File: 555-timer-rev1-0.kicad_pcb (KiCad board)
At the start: 2 copper layers, 19 parts, among them J1 Conn_01x02_Male, SW1 SW_Push, SW2 SW_Push, U1 SA555D

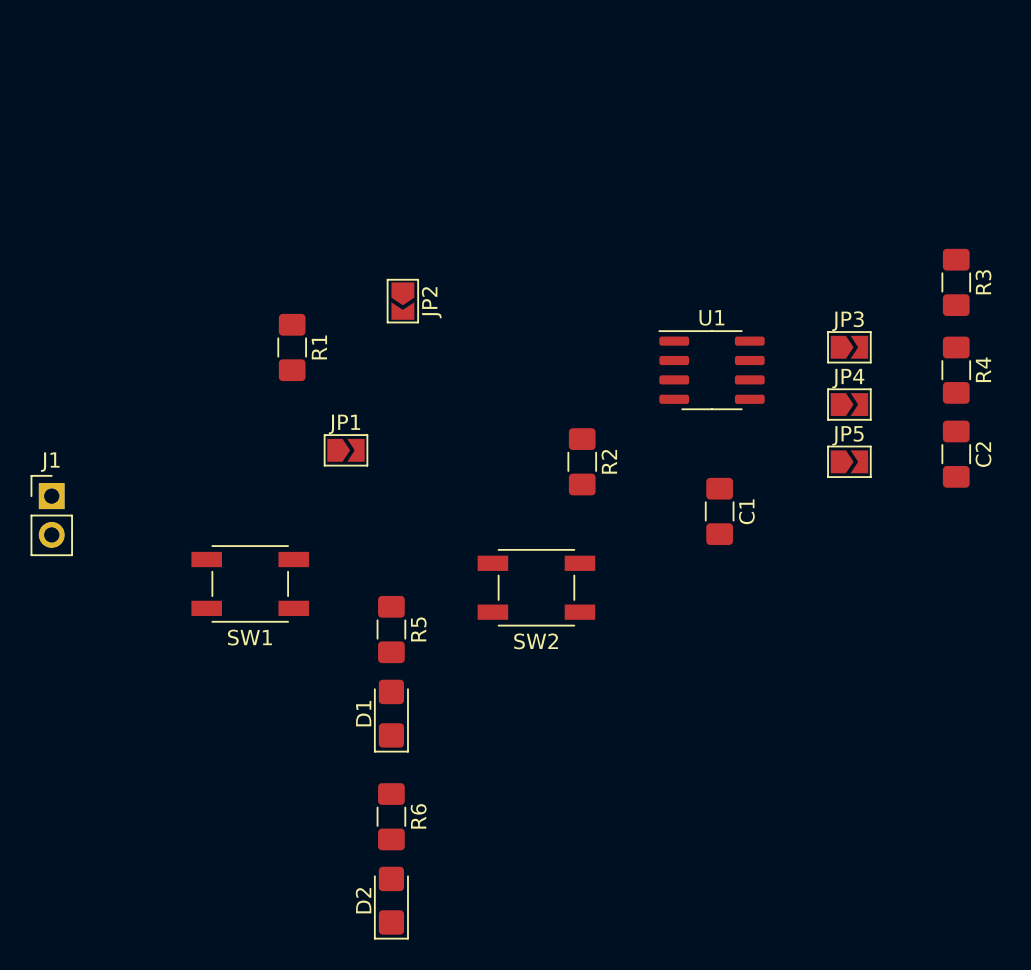
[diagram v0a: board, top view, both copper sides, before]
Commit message: Update PCB layout for 2-layer board.
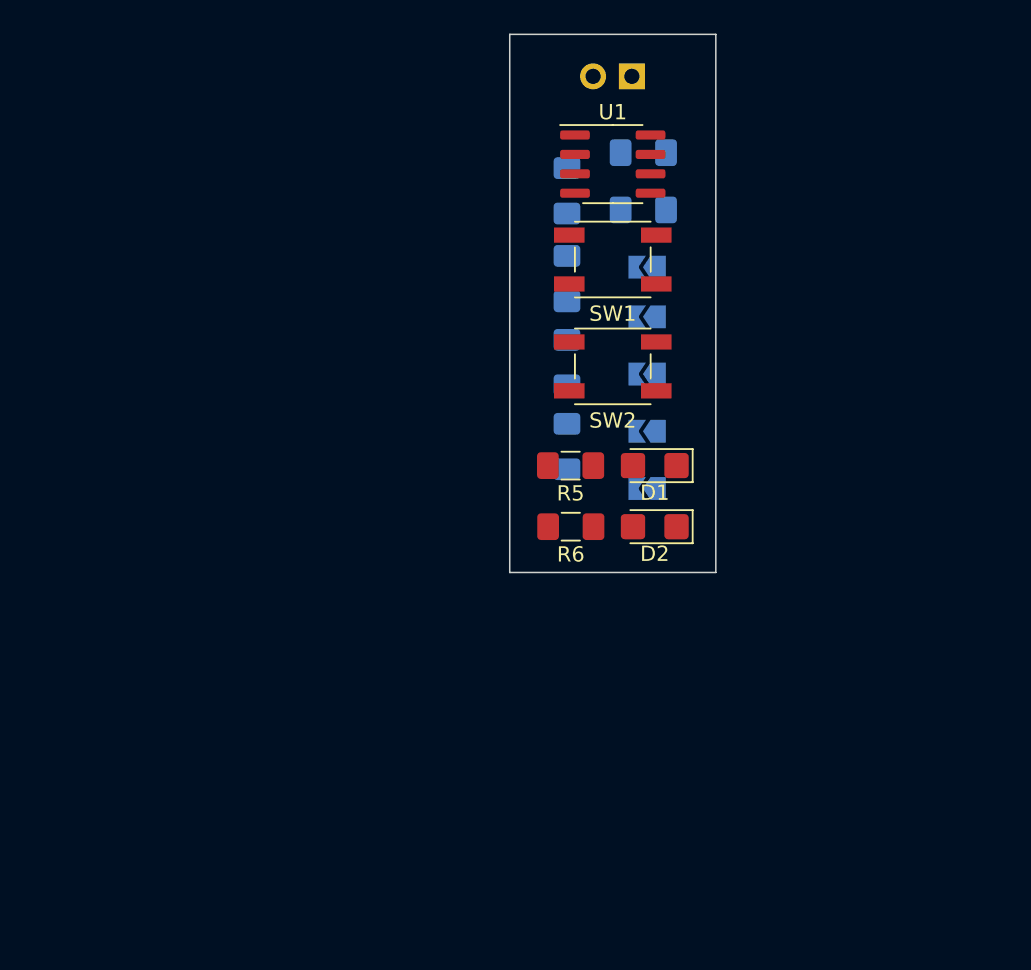
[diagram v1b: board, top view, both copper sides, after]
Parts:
- C1, C2, J1, JP1, JP2, JP3, JP4, JP5, R1, R2, R3, R4: moved to B.Cu
- moved J1 46.9 mm to (150.0, 75.0), turned to 90 degrees
- moved SW1 31.9 mm to (148.8, 87.0)
- moved D2 30.0 mm to (151.5, 104.5), turned to 180 degrees
- moved R1 26.3 mm to (150.8, 80.0), turned to 180 degrees
- moved C2 26.2 mm to (145.8, 93.8)
- moved R3 26.2 mm to (145.8, 82.5)
- moved R4 26.2 mm to (145.8, 88.2)
- moved D1 23.7 mm to (151.5, 100.5), turned to 180 degrees
- moved JP1 23.1 mm to (151.0, 87.5), turned to 180 degrees
- moved R6 22.3 mm to (146.0, 104.5), turned to 180 degrees
- moved JP2 20.2 mm to (151.0, 102.0), turned to 180 degrees
- moved R2 17.0 mm to (150.8, 83.8), turned to 180 degrees
- moved R5 15.9 mm to (146.0, 100.5), turned to 180 degrees
- moved SW2 15.3 mm to (148.8, 94.0)
- moved U1 15.0 mm to (148.8, 80.8)
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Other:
- board outline added: 13.5 x 35.2 mm

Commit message: Finish PCB layout.
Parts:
- moved C1 20.3 mm to (150.5, 79.5), turned to 180 degrees
- moved R2 6.56 mm to (145.8, 79.5), turned to 270 degrees
- moved R5 5.53 mm to (151.5, 100.8), turned to 0 degrees
- moved D1 5.51 mm to (146.0, 100.8), turned to 0 degrees
- moved D2 5.50 mm to (146.0, 104.5), turned to 0 degrees
- moved R6 5.50 mm to (151.5, 104.5), turned to 0 degrees
- moved R1 3.26 mm to (150.5, 83.2)
- moved C2 2.50 mm to (145.8, 96.2)
- moved R3 2.50 mm to (145.8, 85.0)
- moved R4 2.50 mm to (145.8, 90.8)
- moved JP1 0.50 mm to (151.0, 87.0)
- renumbered JP3 to JP2, JP4 to JP3, JP5 to JP4, JP2 to JP5
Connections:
- C2 pad 1: /TRIGGER -> Net-(C2-Pad1)
- JP1 pad 2: Net-(JP1-Pad2) -> /TRIGGER
- JP3 pad 2: /TRIGGER -> Net-(C2-Pad1)
- JP4 pad 2: /TRIGGER -> Net-(C2-Pad1)
- JP5 pad 1: Net-(JP1-Pad1) -> /TRIGGER
- JP5 pad 2: /TRIGGER -> Net-(C2-Pad1)
- R1 pad 1: +5V -> Net-(JP1-Pad1)
- R1 pad 2: Net-(JP1-Pad2) -> +5V
- R4 pad 2: /TRIGGER -> Net-(C2-Pad1)
- R5 pad 1: +5V -> Net-(D1-Pad2)
- R5 pad 2: Net-(D1-Pad2) -> +5V
- R6 pad 1: Net-(D1-Pad1) -> Net-(D2-Pad2)
- R6 pad 2: Net-(D2-Pad2) -> Net-(D1-Pad1)
- SW1 pad 2: Net-(JP1-Pad2) -> Net-(JP1-Pad1)
- U1 pad 2: Net-(JP1-Pad1) -> /TRIGGER
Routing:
- net +5V: track 0.00 -> 54.3 mm
- net GND: track 0.00 -> 53.1 mm, vias 0 -> 1
- net /TRIGGER: track 0.00 -> 40.4 mm, vias 0 -> 1
- net Net-(D1-Pad1): track 0.00 -> 34.3 mm
- net Net-(JP4-Pad1): track 0.00 -> 20.8 mm, vias 0 -> 1
- net Net-(JP2-Pad1): track 0.00 -> 17.2 mm, vias 0 -> 1
- net Net-(R2-Pad2): track 0.00 -> 17.2 mm, vias 0 -> 1
- net Net-(C2-Pad1): track 0.00 -> 14.7 mm
- net Net-(C1-Pad1): track 0.00 -> 11.3 mm, vias 0 -> 1
- net Net-(JP1-Pad1): track 0.00 -> 8.40 mm, vias 0 -> 1
- net Net-(JP2-Pad2): track 0.00 -> 7.92 mm
- net Net-(D1-Pad2): track 0.00 -> 2.60 mm
- net Net-(D2-Pad2): track 0.00 -> 2.59 mm
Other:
- board size 13.5 x 35.2 mm -> 14 x 35.2 mm

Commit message: Add name to silkscreen.
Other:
- board text added: "555 Timer - Rev 1-0 Alexander Fraser 9 Aug 2020"
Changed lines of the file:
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@@
   (general
     (thickness 1.6)
-    (drawings 4)
+    (drawings 5)
     (tracks 110)
     (zones 0)
@@
     )
   )
+  (gr_text "555 Timer - Rev 1-0\nAlexander Fraser\n9 Aug 2020" (at 148.75 105.5) (layer B.SilkS)
+    (effects (font (size 0.5 0.5) (thickness 0.125)) (justify mirror))
+  )
   (gr_line (start 155.75 72.25) (end 155.75 107.5) (layer Edge.Cuts) (width 0.1))

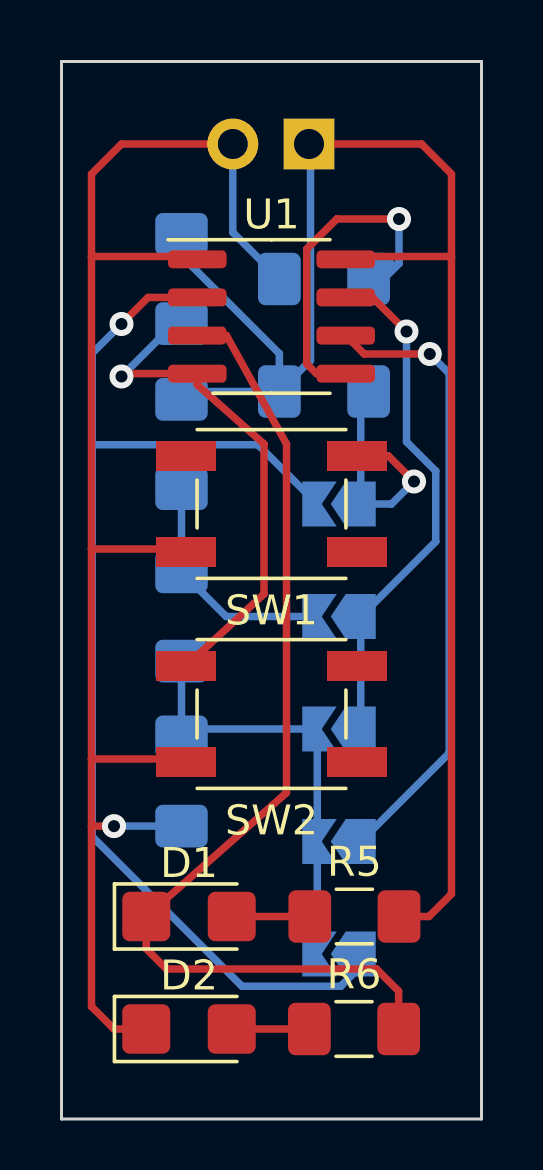
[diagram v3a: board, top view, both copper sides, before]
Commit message: Reverse power rail orientation.
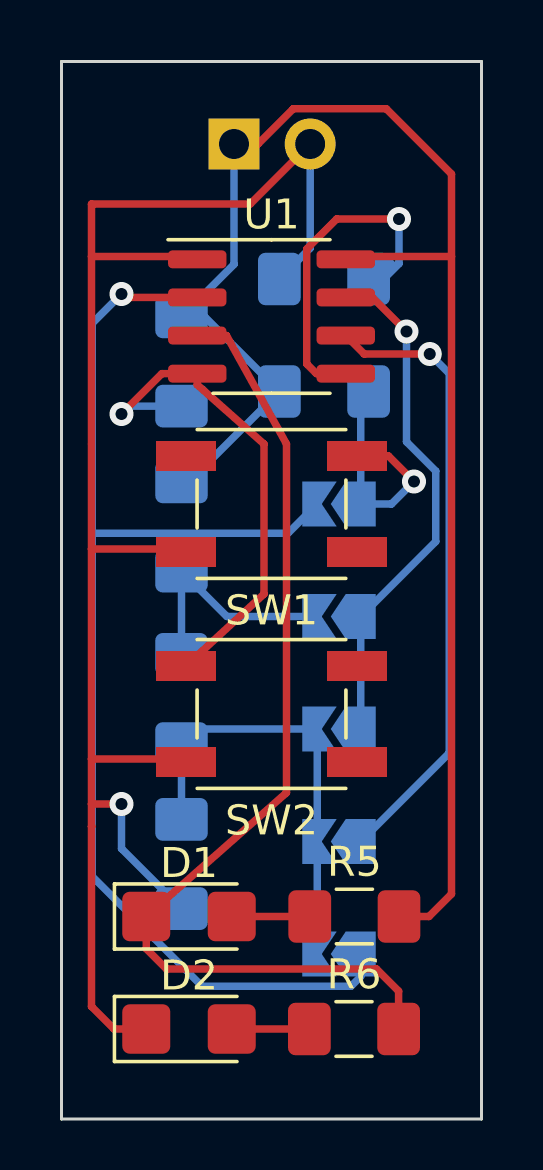
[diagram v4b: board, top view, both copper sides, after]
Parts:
- moved C2 2.75 mm to (145.8, 99.0)
- moved R2 2.75 mm to (145.8, 82.2)
- moved R3 2.75 mm to (145.8, 87.8)
- moved R4 2.75 mm to (145.8, 93.5)
- moved J1 2.50 mm to (147.5, 75.0), turned to 270 degrees
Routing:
- net GND: track 53.1 -> 57.3 mm
- net /TRIGGER: track 40.4 -> 42.1 mm
- net +5V: track 54.3 -> 55.5 mm

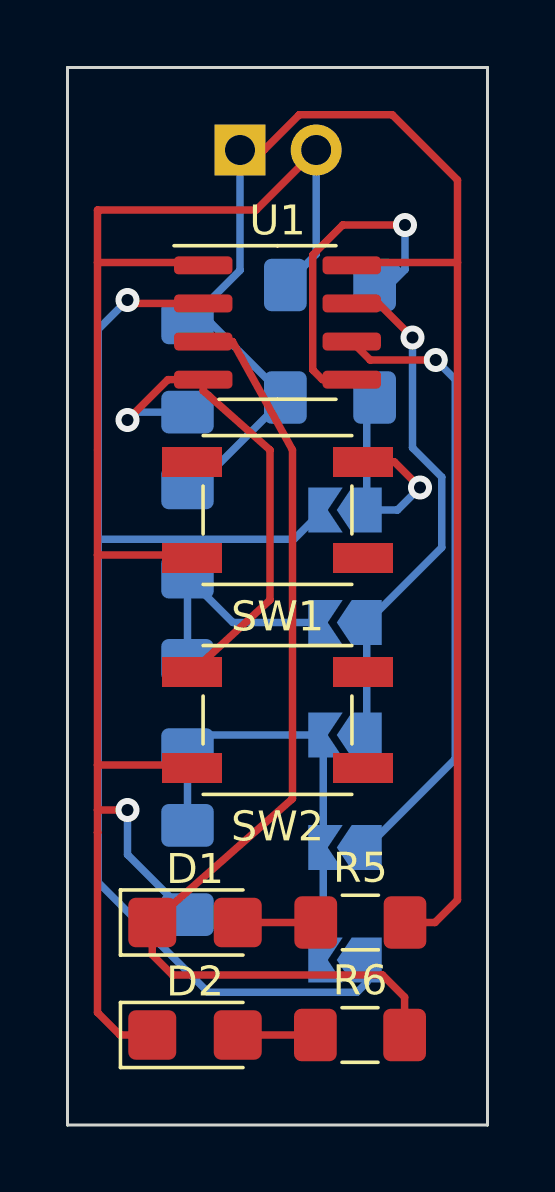
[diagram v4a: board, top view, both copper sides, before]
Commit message: Add VCC and GND fill zones.
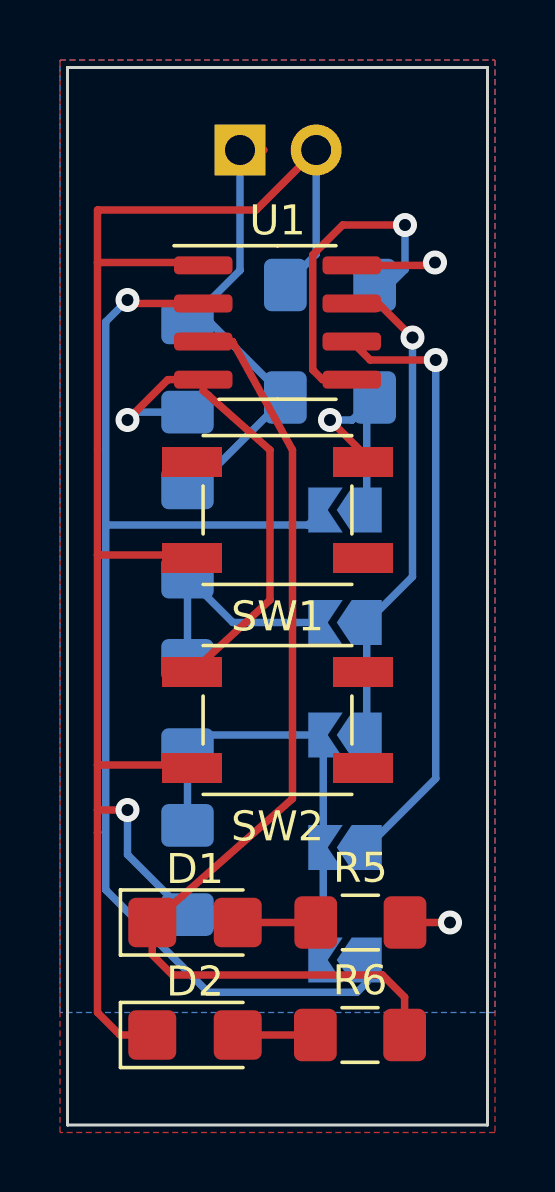
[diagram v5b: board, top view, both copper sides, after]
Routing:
- net +5V: track 55.5 -> 22.5 mm, vias 0 -> 2
- net Net-(JP2-Pad1): track 17.2 -> 16.4 mm
- net Net-(JP1-Pad1): track 8.40 -> 7.72 mm
- net /TRIGGER: track 42.1 -> 41.4 mm
- net Net-(JP4-Pad1): track 20.8 -> 20.3 mm
- added copper zone on B.Cu, net +5V
- added copper zone on F.Cu, net GND
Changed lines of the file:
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@@
     (thickness 1.6)
     (drawings 5)
-    (tracks 117)
+    (tracks 112)
     (zones 0)
     (modules 19)
@@
   (page A4)
   (layers
-    (0 F.Cu signal)
-    (31 B.Cu signal hide)
+    (0 F.Cu signal hide)
+    (31 B.Cu signal)
     (32 B.Adhes user hide)
     (33 F.Adhes user hide)
-    (34 B.Paste user hide)
-    (35 F.Paste user)
-    (36 B.SilkS user hide)
-    (37 F.SilkS user)
-    (38 B.Mask user hide)
-    (39 F.Mask user)
+    (34 B.Paste user)
+    (35 F.Paste user hide)
+    (36 B.SilkS user)
+    (37 F.SilkS user hide)
+    (38 B.Mask user)
+    (39 F.Mask user hide)
     (40 Dwgs.User user hide)
     (41 Cmts.User user hide)
@@
     (44 Edge.Cuts user)
     (45 Margin user hide)
-    (46 B.CrtYd user hide)
-    (47 F.CrtYd user)
-    (48 B.Fab user hide)
-    (49 F.Fab user)
+    (46 B.CrtYd user)
+    (47 F.CrtYd user hide)
+    (48 B.Fab user)
+    (49 F.Fab user hide)
   )
   (setup
@@
   (segment (start 147.25 81.385) (end 149.25 85) (width 0.25) (layer F.Cu) (net 5))
   (segment (start 150.0125 104.5) (end 147.425 104.5) (width 0.25) (layer F.Cu) (net 6))
-  (segment (start 154.75 76) (end 154.75 78.75) (width 0.25) (layer F.Cu) (net 7))
   (segment (start 151.32 78.75) (end 151.225 78.845) (width 0.25) (layer F.Cu) (net 7))
-  (segment (start 154.75 78.75) (end 151.32 78.75) (width 0.25) (layer F.Cu) (net 7))
-  (segment (start 154.75 78.75) (end 154.75 100) (width 0.25) (layer F.Cu) (net 7))
-  (segment (start 154 100.75) (end 153 100.75) (width 0.25) (layer F.Cu) (net 7))
-  (segment (start 154.75 100) (end 154 100.75) (width 0.25) (layer F.Cu) (net 7))
   (segment (start 152.75 78.9875) (end 152.4875 79.25) (width 0.25) (layer B.Cu) (net 2))
   (via (at 153 77.5) (size 0.8) (drill 0.4) (layers F.Cu B.Cu) (net 2))
@@
   (segment (start 142.75 95.5) (end 142.75 97) (width 0.25) (layer F.Cu) (net 1))
   (segment (start 142.75 97) (end 142.75 97.75) (width 0.25) (layer F.Cu) (net 1))
-  (segment (start 150.275 87) (end 149.299999 87.975001) (width 0.25) (layer B.Cu) (net 3))
-  (segment (start 149.299999 87.975001) (end 142.774999 87.975001) (width 0.25) (layer B.Cu) (net 3))
   (via (at 143.75 80) (size 0.8) (drill 0.4) (layers F.Cu B.Cu) (net 3))
   (segment (start 146.275 80.115) (end 143.865 80.115) (width 0.25) (layer F.Cu) (net 3))
   (segment (start 143.865 80.115) (end 143.75 80) (width 0.25) (layer F.Cu) (net 3))
-  (segment (start 142.774999 80.975001) (end 143.75 80) (width 0.25) (layer B.Cu) (net 3))
-  (segment (start 142.774999 87.975001) (end 142.774999 80.975001) (width 0.25) (layer B.Cu) (net 3))
+  (segment (start 151.725 102.75) (end 151.725 102) (width 0.25) (layer B.Cu) (net 3))
   (segment (start 151.39999 103.07501) (end 151.725 102.75) (width 0.25) (layer B.Cu) (net 3))
   (segment (start 146.43682 103.07501) (end 151.39999 103.07501) (width 0.25) (layer B.Cu) (net 3))
-  (segment (start 142.774999 99.413189) (end 146.43682 103.07501) (width 0.25) (layer B.Cu) (net 3))
-  (segment (start 151.725 102.75) (end 151.725 102) (width 0.25) (layer B.Cu) (net 3))
-  (segment (start 142.774999 87.975001) (end 142.774999 99.413189) (width 0.25) (layer B.Cu) (net 3))
+  (segment (start 143.024999 99.663189) (end 146.43682 103.07501) (width 0.25) (layer B.Cu) (net 3))
+  (segment (start 143.75 80) (end 143.024999 80.725001) (width 0.25) (layer B.Cu) (net 3))
+  (segment (start 143.049998 87.5) (end 143.024999 87.524999) (width 0.25) (layer B.Cu) (net 3))
+  (segment (start 150.275 87) (end 149.775 87.5) (width 0.25) (layer B.Cu) (net 3))
+  (segment (start 149.775 87.5) (end 143.049998 87.5) (width 0.25) (layer B.Cu) (net 3))
+  (segment (start 143.024999 80.725001) (end 143.024999 87.524999) (width 0.25) (layer B.Cu) (net 3))
+  (segment (start 143.024999 87.524999) (end 143.024999 99.663189) (width 0.25) (layer B.Cu) (net 3))
   (segment (start 146.0125 86) (end 145.75 86.2625) (width 0.25) (layer B.Cu) (net 7))
   (segment (start 145.75 80.7625) (end 145.75 81.475) (width 0.25) (layer B.Cu) (net 7))
-  (segment (start 148.300998 75) (end 149.475999 73.824999) (width 0.25) (layer F.Cu) (net 7))
   (segment (start 147.5 75) (end 148.300998 75) (width 0.25) (layer F.Cu) (net 7))
-  (segment (start 149.475999 73.824999) (end 152.574999 73.824999) (width 0.25) (layer F.Cu) (net 7))
-  (segment (start 152.574999 73.824999) (end 154.75 76) (width 0.25) (layer F.Cu) (net 7))
   (segment (start 147.5 79.0125) (end 145.75 80.7625) (width 0.25) (layer B.Cu) (net 7))
   (segment (start 147.5 75) (end 147.5 79.0125) (width 0.25) (layer B.Cu) (net 7))
@@
   (segment (start 146 86.2625) (end 149.0125 83.25) (width 0.25) (layer B.Cu) (net 7))
   (segment (start 145.75 86.2625) (end 146 86.2625) (width 0.25) (layer B.Cu) (net 7))
+  (via (at 154.5 100.75) (size 0.8) (drill 0.4) (layers F.Cu B.Cu) (net 7))
+  (segment (start 153 100.75) (end 154.5 100.75) (width 0.25) (layer F.Cu) (net 7))
+  (segment (start 151.225 78.845) (end 153.905 78.845) (width 0.25) (layer F.Cu) (net 7))
+  (via (at 154 78.75) (size 0.8) (drill 0.4) (layers F.Cu B.Cu) (net 7))
+  (segment (start 153.905 78.845) (end 154 78.75) (width 0.25) (layer F.Cu) (net 7))
   (segment (start 151.725 84.0125) (end 152.4875 83.25) (width 0.25) (layer B.Cu) (net 8))
   (segment (start 151.725 87) (end 151.725 84.0125) (width 0.25) (layer B.Cu) (net 8))
-  (via (at 153.5 86.25) (size 0.8) (drill 0.4) (layers F.Cu B.Cu) (net 8))
-  (segment (start 152.75 87) (end 153.5 86.25) (width 0.25) (layer B.Cu) (net 8))
-  (segment (start 151.725 87) (end 152.75 87) (width 0.25) (layer B.Cu) (net 8))
-  (segment (start 152.65 85.4) (end 153.5 86.25) (width 0.25) (layer F.Cu) (net 8))
-  (segment (start 151.6 85.4) (end 152.65 85.4) (width 0.25) (layer F.Cu) (net 8))
+  (via (at 150.5 84) (size 0.8) (drill 0.4) (layers F.Cu B.Cu) (net 8))
+  (segment (start 151.6 85.4) (end 151.6 85.1) (width 0.25) (layer F.Cu) (net 8))
+  (segment (start 151.6 85.1) (end 150.5 84) (width 0.25) (layer F.Cu) (net 8))
+  (segment (start 151.2375 84) (end 151.9875 83.25) (width 0.25) (layer B.Cu) (net 8))
+  (segment (start 150.5 84) (end 151.2375 84) (width 0.25) (layer B.Cu) (net 8))
   (segment (start 145.75 89.2375) (end 145.75 92.0125) (width 0.25) (layer B.Cu) (net 12))
   (segment (start 148.5 85) (end 148.5 90) (width 0.25) (layer F.Cu) (net 9))
@@
   (via (at 153.25 81.25) (size 0.8) (drill 0.4) (layers F.Cu B.Cu) (net 11))
   (segment (start 152.115 80.115) (end 153.25 81.25) (width 0.25) (layer F.Cu) (net 11))
-  (segment (start 154.225001 88.249999) (end 151.725 90.75) (width 0.25) (layer B.Cu) (net 11))
-  (segment (start 154.225001 85.901999) (end 154.225001 88.249999) (width 0.25) (layer B.Cu) (net 11))
-  (segment (start 153.25 84.926998) (end 154.225001 85.901999) (width 0.25) (layer B.Cu) (net 11))
-  (segment (start 153.25 81.25) (end 153.25 84.926998) (width 0.25) (layer B.Cu) (net 11))
+  (segment (start 153.25 89.225) (end 151.725 90.75) (width 0.25) (layer B.Cu) (net 11))
+  (segment (start 153.25 81.25) (end 153.25 89.225) (width 0.25) (layer B.Cu) (net 11))
   (segment (start 147.2625 90.75) (end 145.75 89.2375) (width 0.25) (layer B.Cu) (net 12))
   (segment (start 150.275 90.75) (end 147.2625 90.75) (width 0.25) (layer B.Cu) (net 12))
@@
   (via (at 154.025 82) (size 0.8) (drill 0.4) (layers F.Cu B.Cu) (net 13))
   (segment (start 151.84 82) (end 154.025 82) (width 0.25) (layer F.Cu) (net 13))
-  (segment (start 154.67501 95.29999) (end 151.725 98.25) (width 0.25) (layer B.Cu) (net 13))
-  (segment (start 154.67501 82.65001) (end 154.67501 95.29999) (width 0.25) (layer B.Cu) (net 13))
-  (segment (start 154.025 82) (end 154.67501 82.65001) (width 0.25) (layer B.Cu) (net 13))
+  (segment (start 154.025 95.95) (end 151.725 98.25) (width 0.25) (layer B.Cu) (net 13))
+  (segment (start 154.025 82) (end 154.025 95.95) (width 0.25) (layer B.Cu) (net 13))
+  (zone (net 1) (net_name GND) (layer F.Cu) (hatch edge 0.508)
+    (connect_pads (clearance 0.508))
+    (min_thickness 0.254)
+    (fill yes (arc_segments 32) (thermal_gap 0.508) (thermal_bridge_width 0.508))
+    (polygon
+      (pts
+        (xy 156 107.75) (xy 141.5 107.75) (xy 141.5 72) (xy 156 72)
+      )
+    )
+  )
+  (zone (net 7) (net_name +5V) (layer B.Cu) (hatch edge 0.508)
+    (connect_pads (clearance 0.508))
+    (min_thickness 0.254)
+    (fill yes (arc_segments 32) (thermal_gap 0.508) (thermal_bridge_width 0.508))
+    (polygon
+      (pts
+        (xy 156 103.75) (xy 141.5 103.75) (xy 141.5 72) (xy 156 72)
+      )
+    )
+  )
 )
